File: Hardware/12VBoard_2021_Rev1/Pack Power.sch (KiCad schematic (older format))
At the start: 3 parts

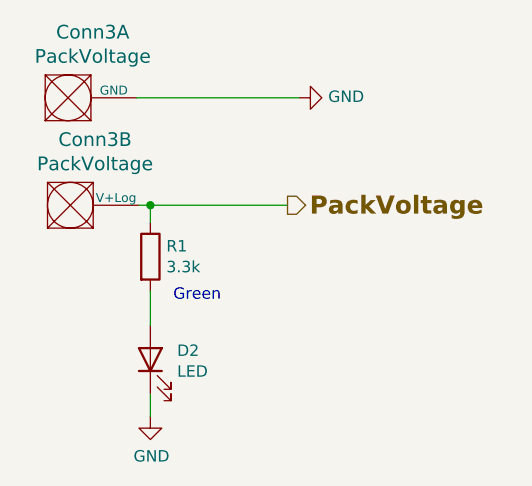
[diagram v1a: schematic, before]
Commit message: Layed out logic power
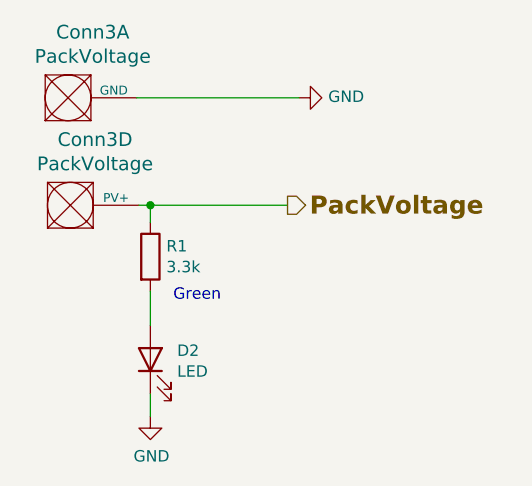
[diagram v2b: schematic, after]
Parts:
- Conn3: footprint MRDT_Connectors:Anderson_2_Horizontal_Side_by_Side -> MRDT_Connectors:Anderson_2_Horizontal_Stacked
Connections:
- net PackVoltage: now also Conn3.4 (PV+); no longer Conn3.2 (V+Log)
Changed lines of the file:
@@
 F 0 "Conn3" H 5148 2967 60  0000 C CNN
 F 1 "PackVoltage" H 5148 2861 60  0000 C CNN
-F 2 "MRDT_Connectors:Anderson_2_Horizontal_Side_by_Side" H 4790 2030 60  0001 C CNN
+F 2 "MRDT_Connectors:Anderson_2_Horizontal_Stacked" H 4790 2030 60  0001 C CNN
 F 3 "" H 4790 2030 60  0001 C CNN
 	1    4940 2580
@@
 $Comp
 L MRDT_Connectors:AndersonPP Conn3
-U 2 1 5F8CAA91
+U 4 1 5F8CAA91
 P 4950 3050
 F 0 "Conn3" H 5158 3437 60  0000 C CNN
 F 1 "PackVoltage" H 5158 3331 60  0000 C CNN
-F 2 "MRDT_Connectors:Anderson_2_Horizontal_Side_by_Side" H 4800 2500 60  0001 C CNN
+F 2 "MRDT_Connectors:Anderson_2_Horizontal_Stacked" H 4800 2500 60  0001 C CNN
 F 3 "" H 4800 2500 60  0001 C CNN
-	2    4950 3050
+	4    4950 3050
 	1    0    0    -1
 $EndComp

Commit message: changed to big bucks
changed to the bucks used in Master due to a realization in the inductor sizing for the LM5116. It would be much bigger than previous years.
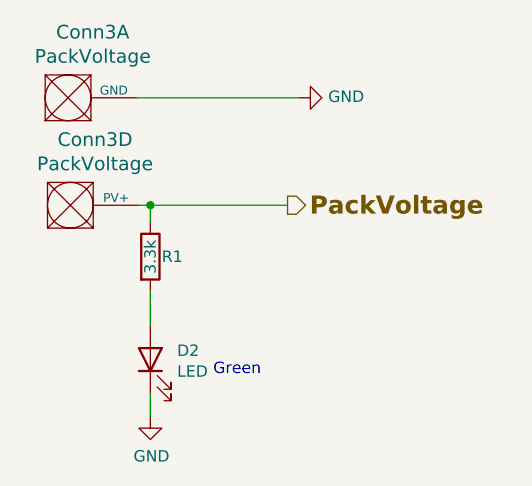
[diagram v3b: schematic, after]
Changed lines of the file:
@@
 $Descr A4 11693 8268
 encoding utf-8
-Sheet 2 9
+Sheet 2 8
 Title ""
 Date ""
@@
 AR Path="/5F74F36B/5F8236F9/5F9524D1" Ref="R?"  Part="1"
 AR Path="/5F8031F1/5F9524D1" Ref="R1"  Part="1"
-F 0 "R1" H 5470 3221 50  0000 L CNN
-F 1 "3.3k" H 5470 3130 50  0000 L CNN
+F 0 "R1" H 5450 3175 50  0000 L CNN
+F 1 "3.3k" V 5400 3100 50  0000 L CNN
 F 2 "Resistor_SMD:R_0603_1608Metric_Pad1.05x0.95mm_HandSolder" V 5330 3175 50  0001 C CNN
 F 3 "~" H 5400 3175 50  0001 C CNN
@@
 Text HLabel 6000 2950 2    79   Output ~ 16
 PackVoltage
-Text Notes 5500 3375 0    50   ~ 0
+Text Notes 5675 3700 0    50   ~ 0
 Green
 Wire Wire Line

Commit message: Started Rev 2
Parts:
- Conn3: footprint MRDT_Connectors:Anderson_2_Horizontal_Stacked -> MRDT_Connectors:Anderson_2_Vertical_Sidy_by_Side
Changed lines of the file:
@@
 F 0 "Conn3" H 5148 2967 60  0000 C CNN
 F 1 "PackVoltage" H 5148 2861 60  0000 C CNN
-F 2 "MRDT_Connectors:Anderson_2_Horizontal_Stacked" H 4790 2030 60  0001 C CNN
+F 2 "MRDT_Connectors:Anderson_2_Vertical_Sidy_by_Side" H 4790 2030 60  0001 C CNN
 F 3 "" H 4790 2030 60  0001 C CNN
 	1    4940 2580
@@
 F 0 "Conn3" H 5158 3437 60  0000 C CNN
 F 1 "PackVoltage" H 5158 3331 60  0000 C CNN
-F 2 "MRDT_Connectors:Anderson_2_Horizontal_Stacked" H 4800 2500 60  0001 C CNN
+F 2 "MRDT_Connectors:Anderson_2_Vertical_Sidy_by_Side" H 4800 2500 60  0001 C CNN
 F 3 "" H 4800 2500 60  0001 C CNN
 	4    4950 3050
